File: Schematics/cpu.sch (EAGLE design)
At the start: 4 parts, among them U1 74HC245N,652, U2 74HC245N,652, U3 74HC245N,652

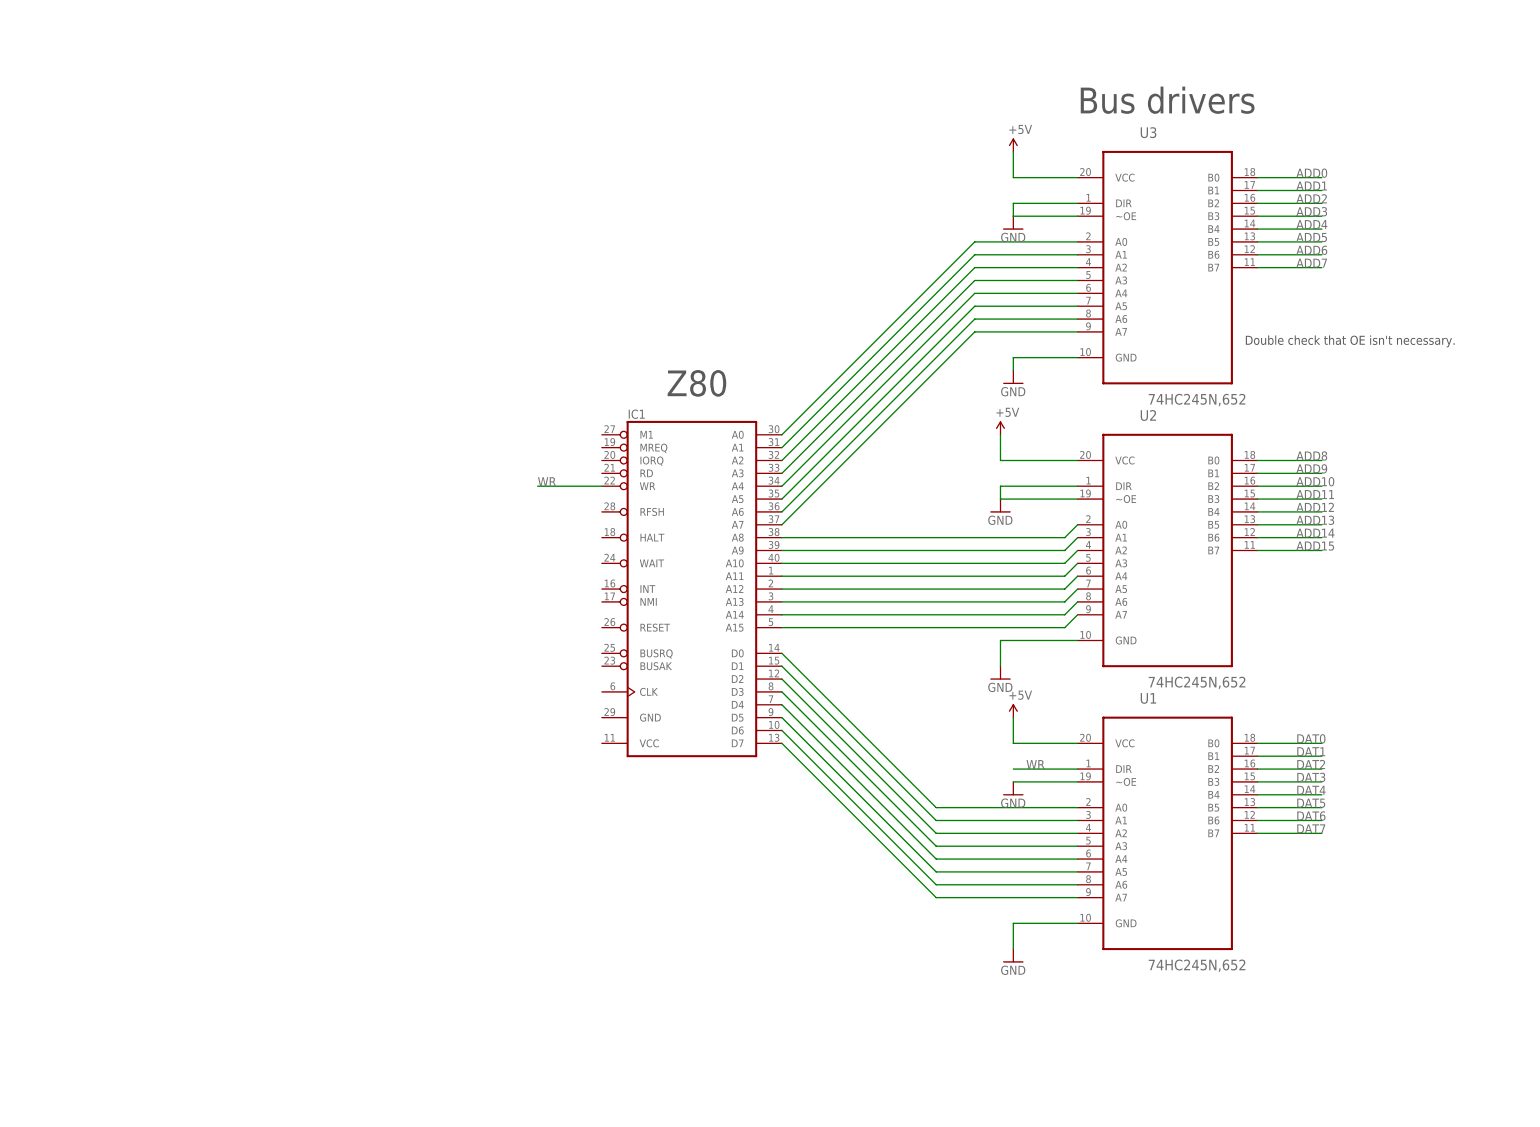
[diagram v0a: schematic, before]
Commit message: Started thinking about clock circuits
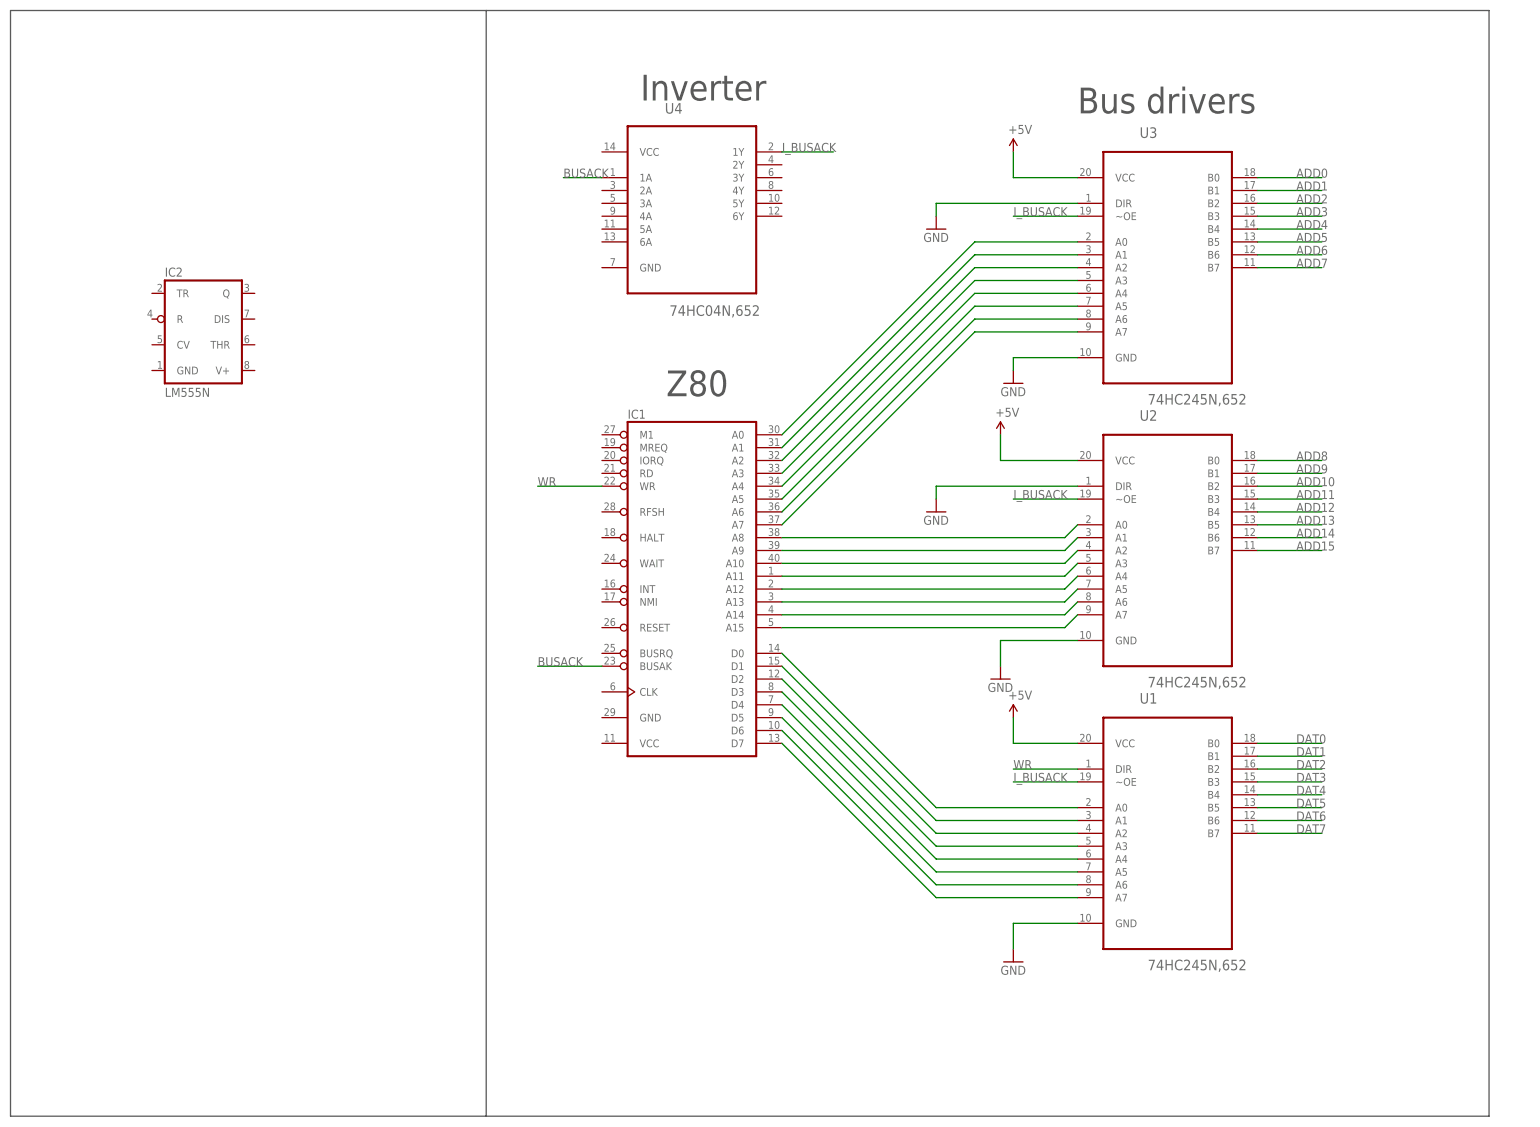
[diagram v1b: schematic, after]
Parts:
- added IC2: LM555N, linear:LM555N
- added U4: 74HC04N,652, NXP_By_element14_Batch_1:74HC04N,652
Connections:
- new net BUSACK: IC1.BUSAK, U4.1A
- new net I_BUSACK: U1.~OE, U2.~OE, U3.~OE, U4.1Y
- net GND: no longer U1.~OE, U2.~OE, U3.~OE
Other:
- note added: "Inverter"
- note removed: "Double check that OE isn't necessary."
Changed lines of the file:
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@@
 <part name="+5V1" library="SparkFun-Aesthetics" deviceset="VCC" device="" value="+5V"/>
 <part name="+5V2" library="SparkFun-Aesthetics" deviceset="VCC" device="" value="+5V"/>
-<part name="GND6" library="SparkFun-Aesthetics" deviceset="GND" device=""/>
+<part name="U4" library="NXP_By_element14_Batch_1" deviceset="74HC04N,652" device=""/>
+<part name="IC2" library="linear" deviceset="*555" device="N" technology="LM"/>
 </parts>
 <sheets>
 <sheet>
 <plain>
-<text x="134.62" y="73.66" size="1.778" layer="97">Double check that OE isn't necessary.</text>
 <text x="101.6" y="119.38" size="5.08" layer="97">Bus drivers</text>
 <text x="20.32" y="63.5" size="5.08" layer="97">Z80</text>
+<text x="15.24" y="121.92" size="5.08" layer="97">Inverter</text>
+<wire x1="-15.24" y1="139.7" x2="182.88" y2="139.7" width="0.1524" layer="97"/>
+<wire x1="182.88" y1="139.7" x2="182.88" y2="-78.74" width="0.1524" layer="97"/>
+<wire x1="182.88" y1="-78.74" x2="-15.24" y2="-78.74" width="0.1524" layer="97"/>
+<wire x1="-15.24" y1="-78.74" x2="-15.24" y2="139.7" width="0.1524" layer="97"/>
+<wire x1="-15.24" y1="139.7" x2="-109.22" y2="139.7" width="0.1524" layer="97"/>
+<wire x1="-109.22" y1="139.7" x2="-109.22" y2="-78.74" width="0.1524" layer="97"/>
+<wire x1="-109.22" y1="-78.74" x2="-15.24" y2="-78.74" width="0.1524" layer="97"/>
 </plain>
 <instances>
@@
 <instance part="U2" gate="A" x="119.38" y="35.56"/>
 <instance part="U3" gate="A" x="119.38" y="91.44"/>
-<instance part="GND1" gate="1" x="86.36" y="40.64"/>
+<instance part="GND1" gate="1" x="73.66" y="40.64"/>
 <instance part="GND2" gate="1" x="86.36" y="7.62"/>
 <instance part="GND3" gate="1" x="88.9" y="-48.26"/>
 <instance part="GND4" gate="1" x="88.9" y="66.04"/>
-<instance part="GND5" gate="1" x="88.9" y="96.52"/>
+<instance part="GND5" gate="1" x="73.66" y="96.52"/>
 <instance part="+5V" gate="G$1" x="88.9" y="0"/>
 <instance part="+5V1" gate="G$1" x="86.36" y="55.88"/>
 <instance part="+5V2" gate="G$1" x="88.9" y="111.76"/>
-<instance part="GND6" gate="1" x="88.9" y="-15.24"/>
+<instance part="U4" gate="A" x="25.4" y="104.14"/>
+<instance part="IC2" gate="A" x="-71.12" y="76.2"/>
 </instances>
 <busses>
@@
 <pinref part="U1" gate="A" pin="DIR"/>
 <wire x1="101.6" y1="-10.16" x2="88.9" y2="-10.16" width="0.1524" layer="91"/>
-<label x="91.44" y="-10.16" size="1.778" layer="95"/>
+<label x="88.9" y="-10.16" size="1.778" layer="95"/>
 </segment>
 </net>
@@
 <segment>
 <pinref part="U2" gate="A" pin="DIR"/>
-<wire x1="101.6" y1="45.72" x2="86.36" y2="45.72" width="0.1524" layer="91"/>
-<wire x1="86.36" y1="45.72" x2="86.36" y2="43.18" width="0.1524" layer="91"/>
+<wire x1="101.6" y1="45.72" x2="73.66" y2="45.72" width="0.1524" layer="91"/>
+<wire x1="73.66" y1="45.72" x2="73.66" y2="43.18" width="0.1524" layer="91"/>
 <pinref part="GND1" gate="1" pin="GND"/>
-<pinref part="U2" gate="A" pin="~OE"/>
-<wire x1="101.6" y1="43.18" x2="86.36" y2="43.18" width="0.1524" layer="91"/>
 </segment>
 <segment>
@@
 </segment>
 <segment>
-<pinref part="U3" gate="A" pin="DIR"/>
-<pinref part="GND5" gate="1" pin="GND"/>
-<wire x1="101.6" y1="101.6" x2="88.9" y2="101.6" width="0.1524" layer="91"/>
-<wire x1="88.9" y1="101.6" x2="88.9" y2="99.06" width="0.1524" layer="91"/>
-<pinref part="U3" gate="A" pin="~OE"/>
-<wire x1="101.6" y1="99.06" x2="88.9" y2="99.06" width="0.1524" layer="91"/>
-</segment>
-<segment>
 <pinref part="U3" gate="A" pin="GND"/>
 <pinref part="GND4" gate="1" pin="GND"/>
@@
 </segment>
 <segment>
-<pinref part="U1" gate="A" pin="~OE"/>
-<wire x1="101.6" y1="-12.7" x2="88.9" y2="-12.7" width="0.1524" layer="91"/>
-<pinref part="GND6" gate="1" pin="GND"/>
+<pinref part="U3" gate="A" pin="DIR"/>
+<pinref part="GND5" gate="1" pin="GND"/>
+<wire x1="101.6" y1="101.6" x2="73.66" y2="101.6" width="0.1524" layer="91"/>
+<wire x1="73.66" y1="101.6" x2="73.66" y2="99.06" width="0.1524" layer="91"/>
 </segment>
 </net>
@@
 </segment>
 </net>
+<net name="BUSACK" class="0">
+<segment>
+<pinref part="IC1" gate="1" pin="BUSAK"/>
+<wire x1="7.62" y1="10.16" x2="-5.08" y2="10.16" width="0.1524" layer="91"/>
+<label x="-5.08" y="10.16" size="1.778" layer="95"/>
+</segment>
+<segment>
+<pinref part="U4" gate="A" pin="1A"/>
+<wire x1="0" y1="106.68" x2="7.62" y2="106.68" width="0.1524" layer="91"/>
+<label x="0" y="106.68" size="1.778" layer="95"/>
+</segment>
+</net>
+<net name="I_BUSACK" class="0">
+<segment>
+<pinref part="U4" gate="A" pin="1Y"/>
+<wire x1="43.18" y1="111.76" x2="53.34" y2="111.76" width="0.1524" layer="91"/>
+<label x="43.18" y="111.76" size="1.778" layer="95"/>
+</segment>
+<segment>
+<pinref part="U3" gate="A" pin="~OE"/>
+<wire x1="101.6" y1="99.06" x2="88.9" y2="99.06" width="0.1524" layer="91"/>
+<label x="88.9" y="99.06" size="1.778" layer="95"/>
+</segment>
+<segment>
+<pinref part="U2" gate="A" pin="~OE"/>
+<wire x1="101.6" y1="43.18" x2="88.9" y2="43.18" width="0.1524" layer="91"/>
+<label x="88.9" y="43.18" size="1.778" layer="95"/>
+</segment>
+<segment>
+<pinref part="U1" gate="A" pin="~OE"/>
+<wire x1="101.6" y1="-12.7" x2="88.9" y2="-12.7" width="0.1524" layer="91"/>
+<label x="88.9" y="-12.7" size="1.778" layer="95"/>
+</segment>
+</net>

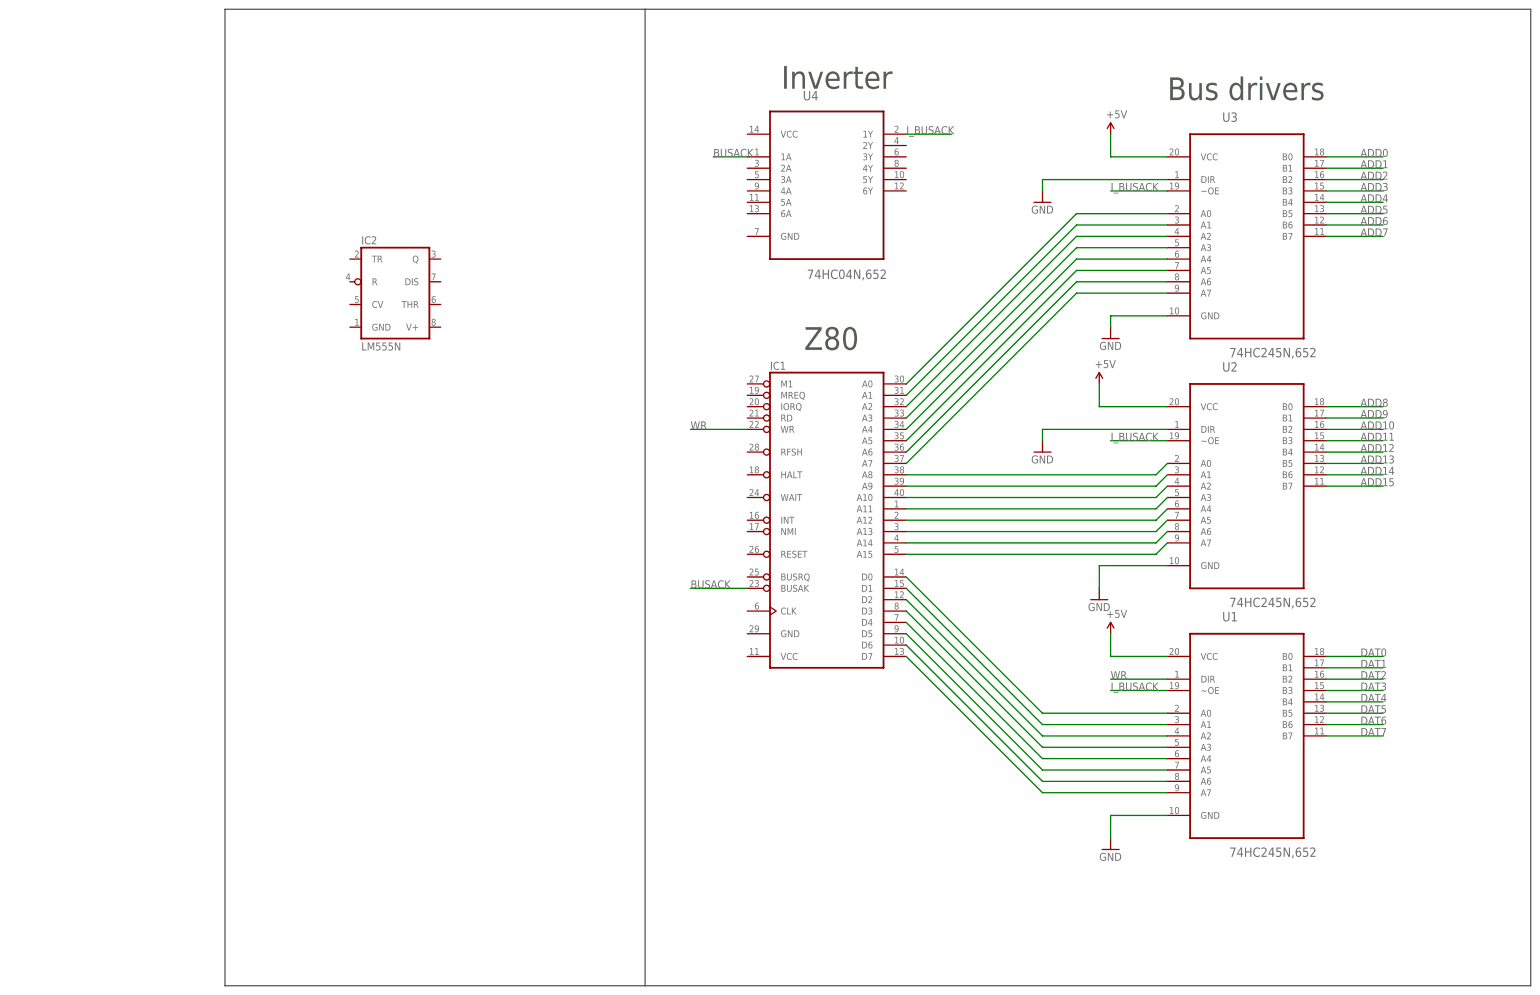
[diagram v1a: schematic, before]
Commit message: added clock circuits
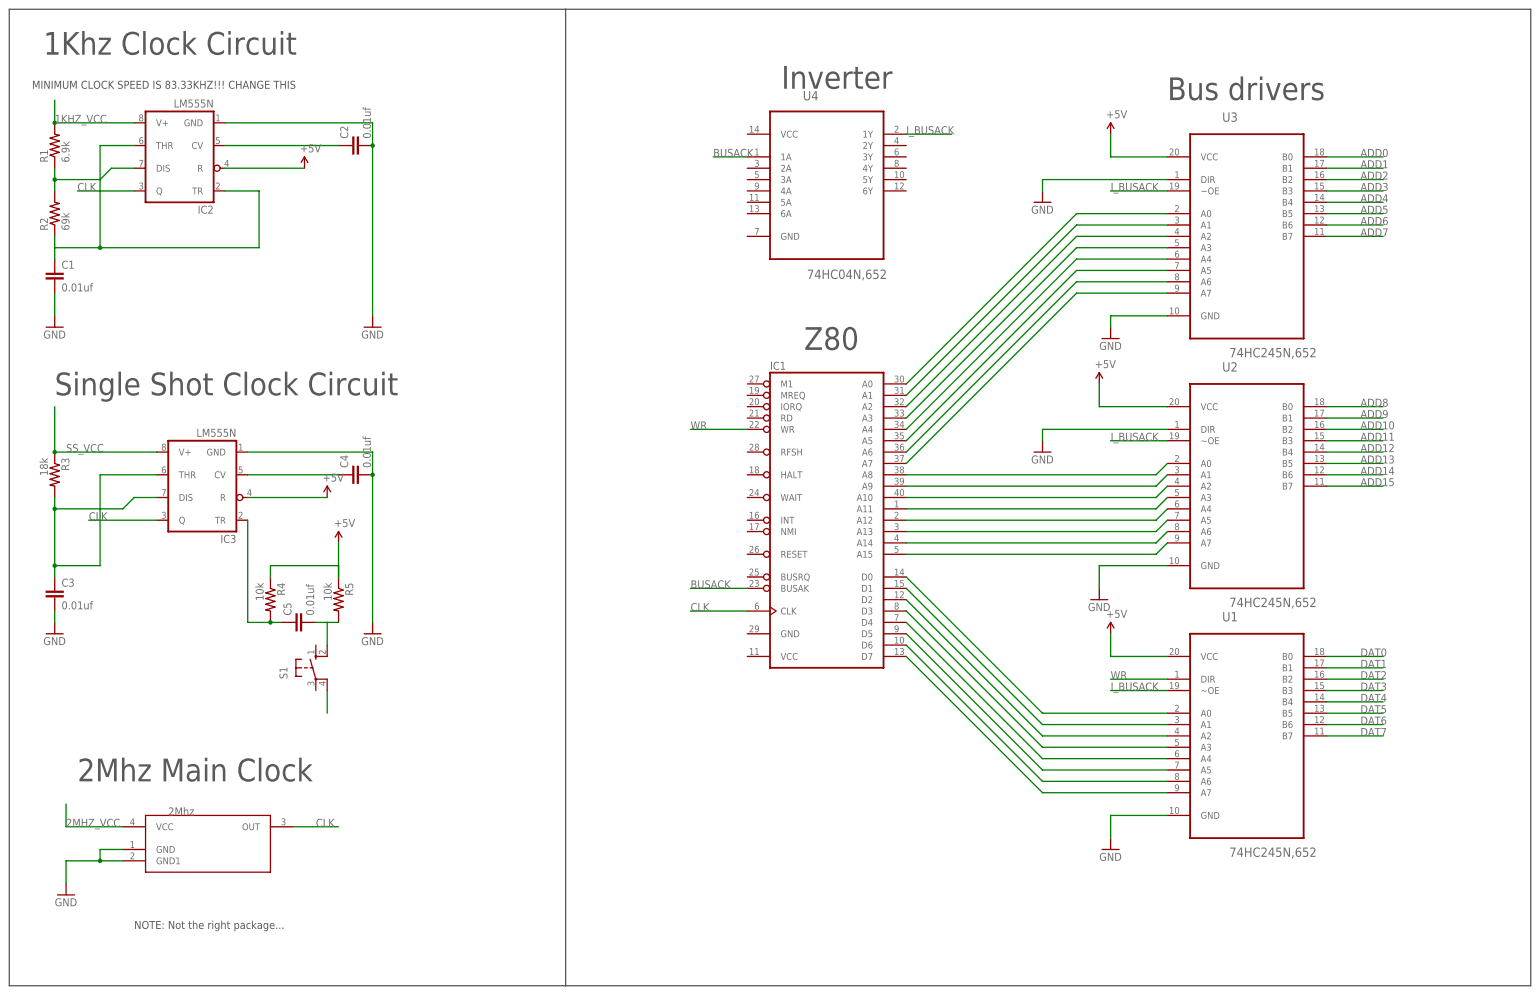
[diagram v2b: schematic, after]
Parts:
- added C1, C2, C3, C4, C5: 0.01uf, SparkFun-Capacitors:CAP0805
- added IC3: LM555N, linear:LM555N
- added R1: 6.9k, SparkFun-Resistors:RESISTOR0805-RES
- added R2: 69k, SparkFun-Resistors:RESISTOR0805-RES
- added R3: 18k, SparkFun-Resistors:RESISTOR0805-RES
- added R4, R5: 10k, SparkFun-Resistors:RESISTOR0805-RES
- added S1: (no value), switch-omron:10-XX
- added U$1: 2Mhz, JakeBooth:OSCILLATOR
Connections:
- new net 1KHZ_VCC: IC2.V+, R1.2
- new net 2MHZ_VCC: U$1.VCC
- new net CLK: IC1.CLK, IC2.Q, IC3.Q, U$1.OUT
- new net N$25: IC2.DIS, R1.1, R2.2
- new net N$26: C1.1, IC2.THR, IC2.TR, R2.1
- new net N$27: C4.1, IC3.CV
- new net N$28: C2.1, IC2.CV
- new net N$29: C3.1, IC3.DIS, IC3.THR, R3.2
- new net N$30: C5.1, IC3.TR, R4.2
- new net N$31: C5.2, R5.2, S1.S1
- new net N$33: S1.P1
- new net SS_VCC: IC3.V+, R3.1
- net GND: now also C1.2, C2.2, C3.2, C4.2, IC2.GND, IC3.GND, U$1.GND, U$1.GND1
- net VCC: now also IC2.R, IC3.R, R4.1, R5.1
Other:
- note added: "1Khz Clock Circuit"
- note added: "2Mhz"
- note added: "2Mhz Main Clock"
- note added: "MINIMUM CLOCK SPEED IS 83.33KHZ!!! CHANGE THIS"
- note added: "NOTE: Not the right package..."
- note added: "Single Shot Clock Circuit"
- moved on the sheet: IC2
